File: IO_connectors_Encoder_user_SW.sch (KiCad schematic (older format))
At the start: 36 parts, among them IC1 TPD4E001DRLR, IC2 74AUP1G74DC.125, IC3 CD74HC4050PWR, SW1 TL1100CF160Q, SW2 PEC16-2215F-S0024, X1 DS1024-2*20R0, X2 DS1013-16SSIB1, X3 691322110005

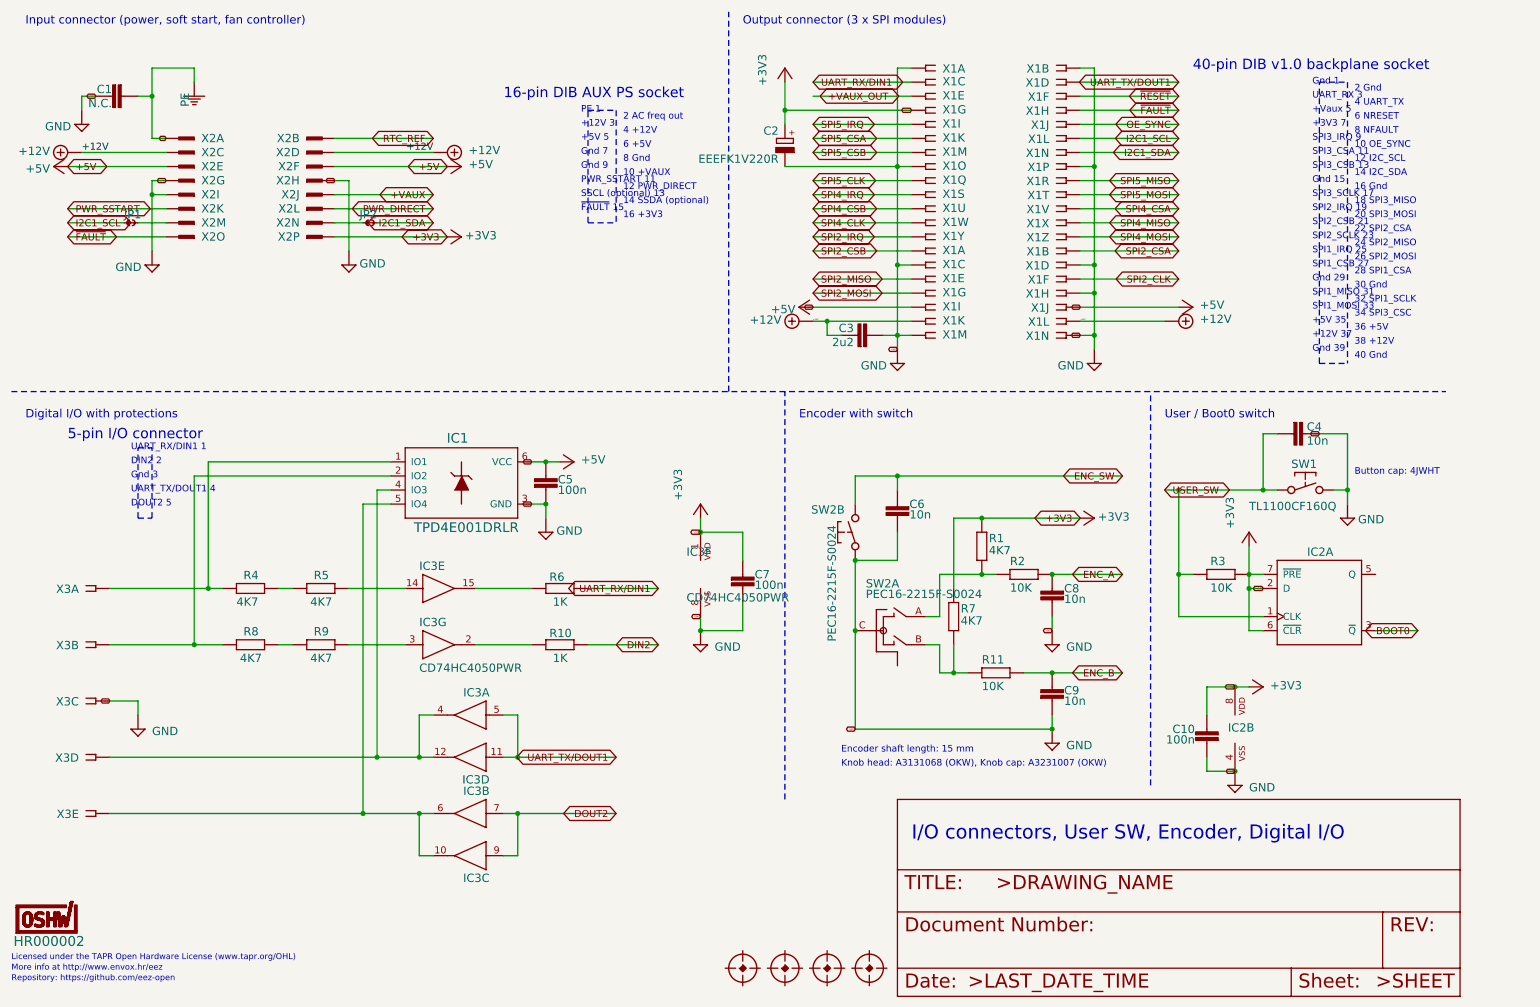
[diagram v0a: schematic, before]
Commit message: Assigning parts - netlitst to pcb
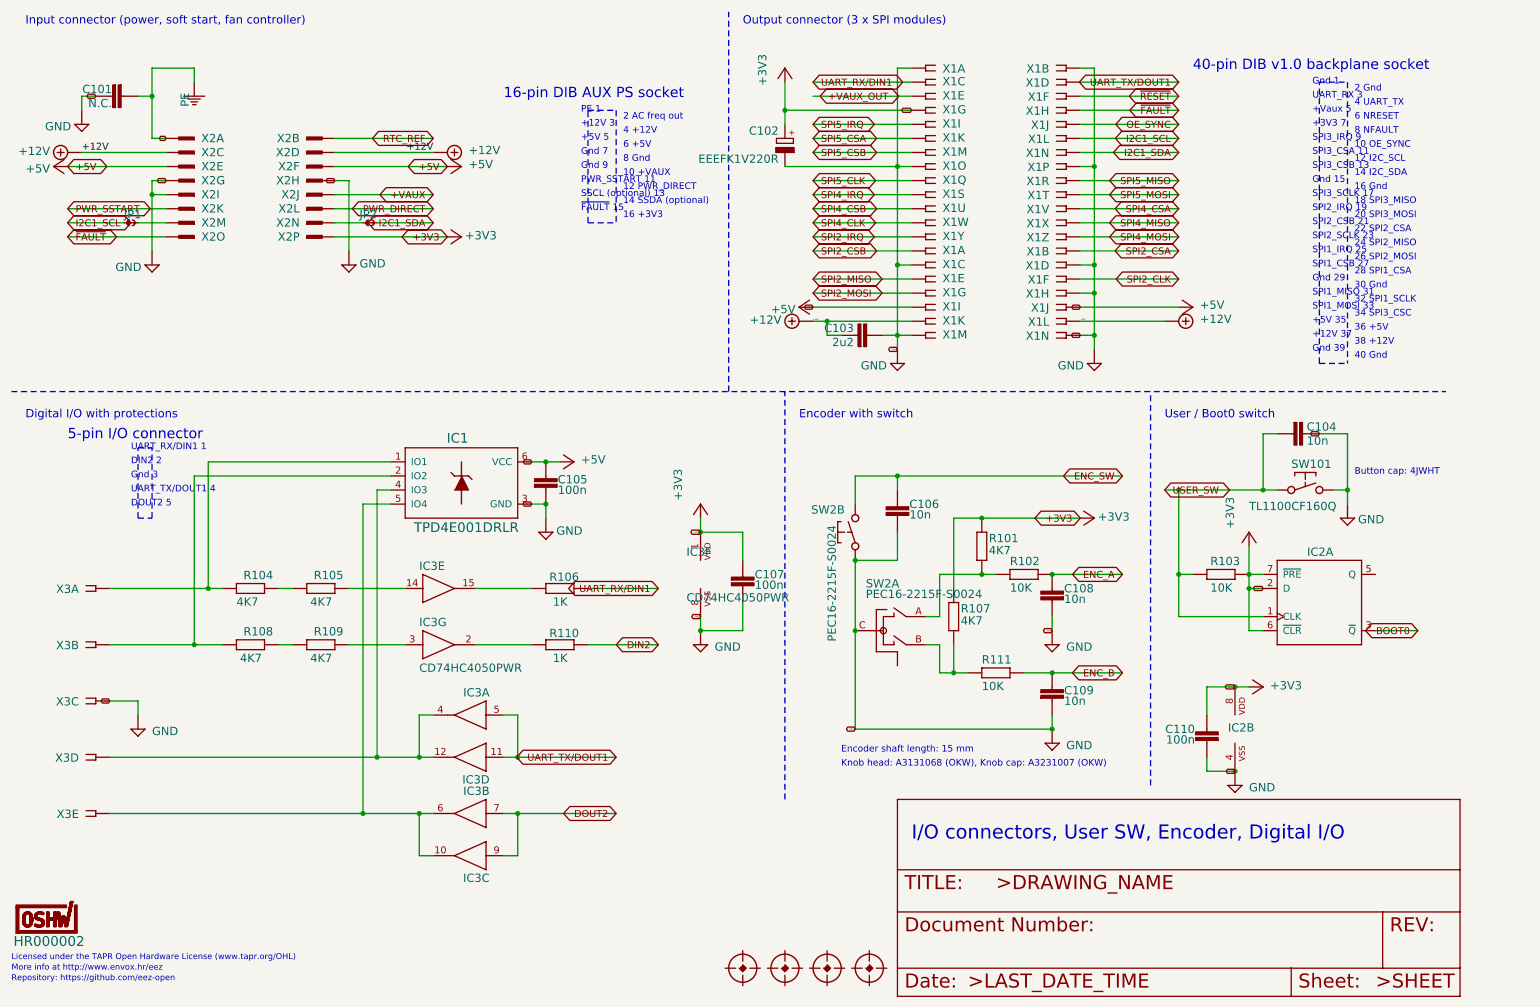
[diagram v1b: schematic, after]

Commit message: New annotation - All STM32 parts are +100
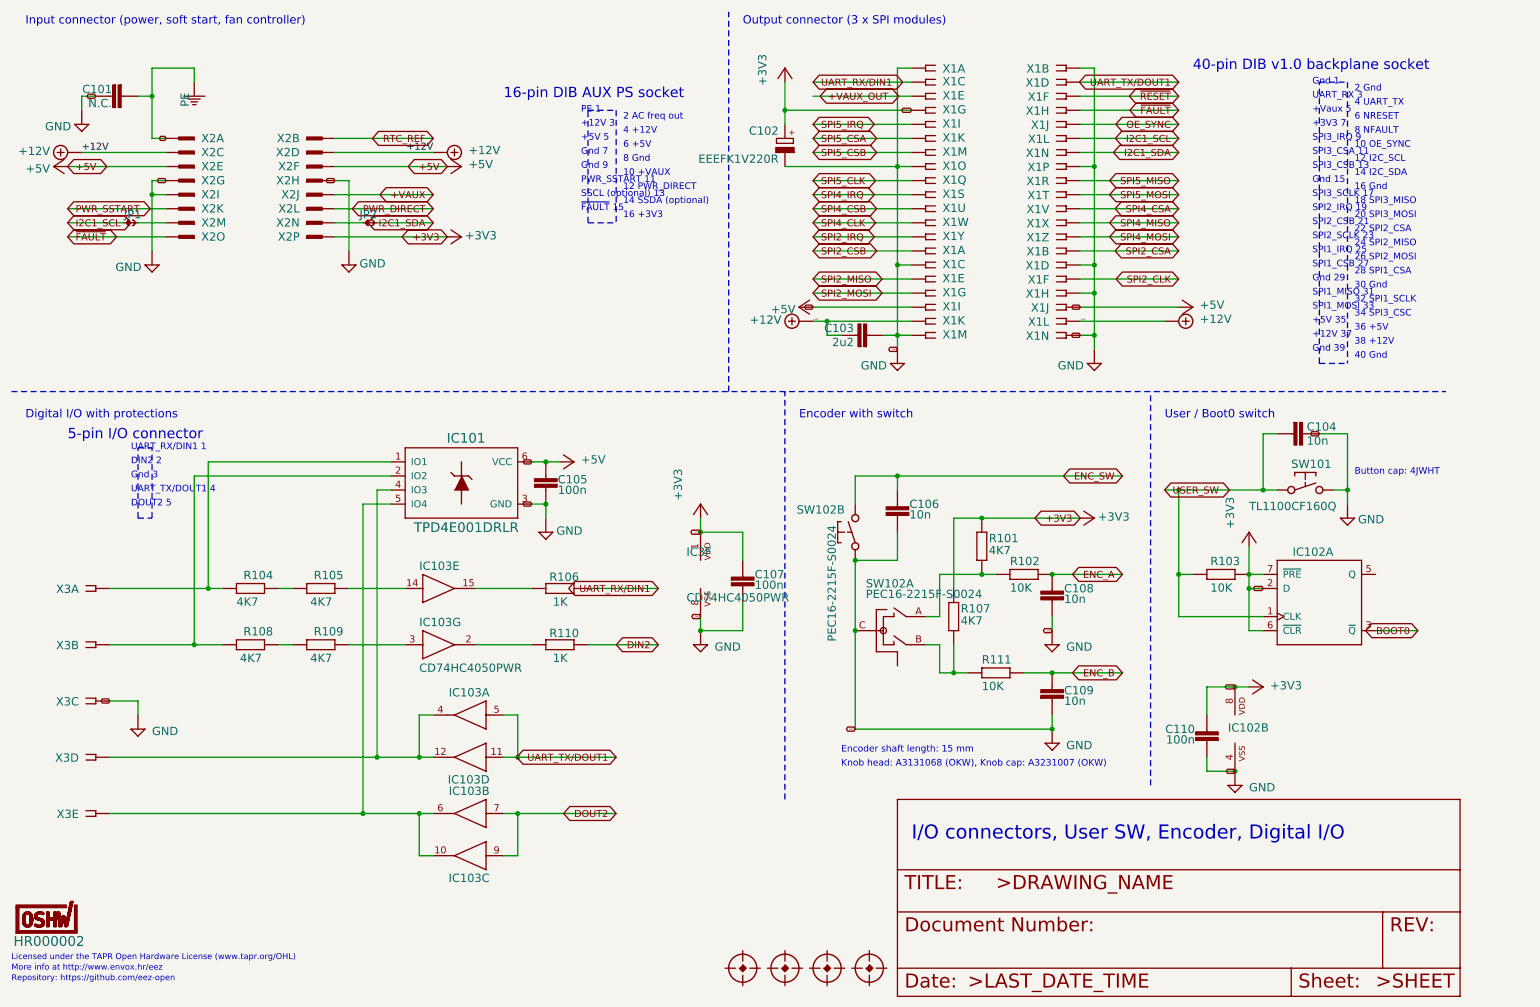
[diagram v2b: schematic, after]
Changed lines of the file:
@@
 EESchema Schematic File Version 4
-LIBS:ulx3s-cache
-EELAYER 29 0
+EELAYER 30 0
 EELAYER END
 $Descr User 12131 8568
@@
 AR Path="/C308D36B2E8B8105" Ref="SW2"  Part="1"
 AR Path="/5F88C8A0/C308D36B2E8B8105" Ref="SW2"  Part="1"
-AR Path="/5F8FDB74/2E8B8105" Ref="SW2"  Part="1"
-F 0 "SW2" H 7075 5400 59  0000 L BNN
+AR Path="/5F8FDB74/2E8B8105" Ref="SW102"  Part="1"
+F 0 "SW102" H 7075 5400 59  0000 L BNN
 F 1 "PEC16-2215F-S0024" H 7075 5325 59  0000 L BNN
 F 2 "EEZ DIB MCU r3B4:PEC16-2215F" H 7100 5100 50  0001 C CNN
@@
 AR Path="/C308D36B2E8B8109" Ref="SW2"  Part="2"
 AR Path="/5F88C8A0/C308D36B2E8B8109" Ref="SW2"  Part="2"
-AR Path="/5F8FDB74/2E8B8109" Ref="SW2"  Part="2"
-F 0 "SW2" V 7125 4475 59  0000 L TNN
+AR Path="/5F8FDB74/2E8B8109" Ref="SW102"  Part="2"
+F 0 "SW102" V 7125 4475 59  0000 L TNN
 F 1 "PEC16-2215F-S0024" H 7050 4600 59  0000 R TNN
 F 2 "EEZ DIB MCU r3B4:PEC16-2215F" H 7000 4400 50  0001 C CNN
@@
 AR Path="/B33006915ED25CA7" Ref="IC3"  Part="1"
 AR Path="/5F88C8A0/B33006915ED25CA7" Ref="IC3"  Part="1"
-AR Path="/5F8FDB74/5ED25CA7" Ref="IC3"  Part="1"
-F 0 "IC3" H 4200 5825 59  0000 L BNN
+AR Path="/5F8FDB74/5ED25CA7" Ref="IC103"  Part="1"
+F 0 "IC103" H 4200 5825 59  0000 L BNN
 F 1 "CD74HC4050PWR" H 4200 5500 59  0001 L BNN
 F 2 "EEZ DIB MCU r3B4:PW16" H 4300 5700 50  0001 C CNN
@@
 AR Path="/B33006915ED25CAB" Ref="IC3"  Part="2"
 AR Path="/5F88C8A0/B33006915ED25CAB" Ref="IC3"  Part="2"
-AR Path="/5F8FDB74/5ED25CAB" Ref="IC3"  Part="2"
-F 0 "IC3" H 4200 6525 59  0000 L BNN
+AR Path="/5F8FDB74/5ED25CAB" Ref="IC103"  Part="2"
+F 0 "IC103" H 4200 6525 59  0000 L BNN
 F 1 "CD74HC4050PWR" H 4200 6200 59  0001 L BNN
 F 2 "EEZ DIB MCU r3B4:PW16" H 4300 6400 50  0001 C CNN
@@
 AR Path="/B33006915ED25CAF" Ref="IC3"  Part="3"
 AR Path="/5F88C8A0/B33006915ED25CAF" Ref="IC3"  Part="3"
-AR Path="/5F8FDB74/5ED25CAF" Ref="IC3"  Part="3"
-F 0 "IC3" H 4200 6825 59  0000 L BNN
+AR Path="/5F8FDB74/5ED25CAF" Ref="IC103"  Part="3"
+F 0 "IC103" H 4200 6825 59  0000 L BNN
 F 1 "CD74HC4050PWR" H 4200 6500 59  0001 L BNN
 F 2 "EEZ DIB MCU r3B4:PW16" H 4300 6700 50  0001 C CNN
@@
 AR Path="/B33006915ED25CB3" Ref="IC3"  Part="4"
 AR Path="/5F88C8A0/B33006915ED25CB3" Ref="IC3"  Part="4"
-AR Path="/5F8FDB74/5ED25CB3" Ref="IC3"  Part="4"
-F 0 "IC3" H 4200 6125 59  0000 L BNN
+AR Path="/5F8FDB74/5ED25CB3" Ref="IC103"  Part="4"
+F 0 "IC103" H 4200 6125 59  0000 L BNN
 F 1 "CD74HC4050PWR" H 4200 5800 59  0001 L BNN
 F 2 "EEZ DIB MCU r3B4:PW16" H 4300 6000 50  0001 C CNN
@@
 AR Path="/B33006915ED25CBF" Ref="IC3"  Part="7"
 AR Path="/5F88C8A0/B33006915ED25CBF" Ref="IC3"  Part="7"
-AR Path="/5F8FDB74/5ED25CBF" Ref="IC3"  Part="7"
-F 0 "IC3" H 3900 5325 59  0000 L BNN
+AR Path="/5F8FDB74/5ED25CBF" Ref="IC103"  Part="7"
+F 0 "IC103" H 3900 5325 59  0000 L BNN
 F 1 "CD74HC4050PWR" H 3900 5000 59  0000 L BNN
 F 2 "EEZ DIB MCU r3B4:PW16" H 4000 5200 50  0001 C CNN
@@
 AR Path="/B33006915ED25CB7" Ref="IC3"  Part="5"
 AR Path="/5F88C8A0/B33006915ED25CB7" Ref="IC3"  Part="5"
-AR Path="/5F8FDB74/5ED25CB7" Ref="IC3"  Part="5"
-F 0 "IC3" H 3900 4925 59  0000 L BNN
+AR Path="/5F8FDB74/5ED25CB7" Ref="IC103"  Part="5"
+F 0 "IC103" H 3900 4925 59  0000 L BNN
 F 1 "CD74HC4050PWR" H 3900 4600 59  0001 L BNN
 F 2 "EEZ DIB MCU r3B4:PW16" H 4000 4800 50  0001 C CNN
@@
 AR Path="/A199DC2541D8E9F" Ref="IC1"  Part="1"
 AR Path="/5F88C8A0/A199DC2541D8E9F" Ref="IC1"  Part="1"
-AR Path="/5F8FDB74/541D8E9F" Ref="IC1"  Part="1"
-F 0 "IC1" H 4095 4228 69  0000 L BNN
+AR Path="/5F8FDB74/541D8E9F" Ref="IC101"  Part="1"
+F 0 "IC101" H 4095 4228 69  0000 L BNN
 F 1 "TPD4E001DRLR" H 3862 3593 69  0000 L BNN
 F 2 "EEZ DIB MCU r3B4:DRL6" H 4200 4000 50  0001 C CNN
@@
 AR Path="/279C899179298246" Ref="IC2"  Part="1"
 AR Path="/5F88C8A0/279C899179298246" Ref="IC2"  Part="1"
-AR Path="/5F8FDB74/79298246" Ref="IC2"  Part="1"
-F 0 "IC2" H 10400 5225 59  0000 R BNN
+AR Path="/5F8FDB74/79298246" Ref="IC102"  Part="1"
+F 0 "IC102" H 10400 5225 59  0000 R BNN
 F 1 "74AUP1G74DC.125" H 9900 4500 59  0001 L BNN
 F 2 "EEZ DIB MCU r3B4:DCU8" H 10300 4900 50  0001 C CNN
@@
 AR Path="/279C89917929824A" Ref="IC2"  Part="2"
 AR Path="/5F88C8A0/279C89917929824A" Ref="IC2"  Part="2"
-AR Path="/5F8FDB74/7929824A" Ref="IC2"  Part="2"
-F 0 "IC2" H 9650 5775 59  0000 L BNN
+AR Path="/5F8FDB74/7929824A" Ref="IC102"  Part="2"
+F 0 "IC102" H 9650 5775 59  0000 L BNN
 F 1 "74AUP1G74DC.125" H 9400 5400 59  0001 L BNN
 F 2 "EEZ DIB MCU r3B4:DCU8" H 9700 5800 50  0001 C CNN

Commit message: All STM32 parts are now +100, moving parts to original position
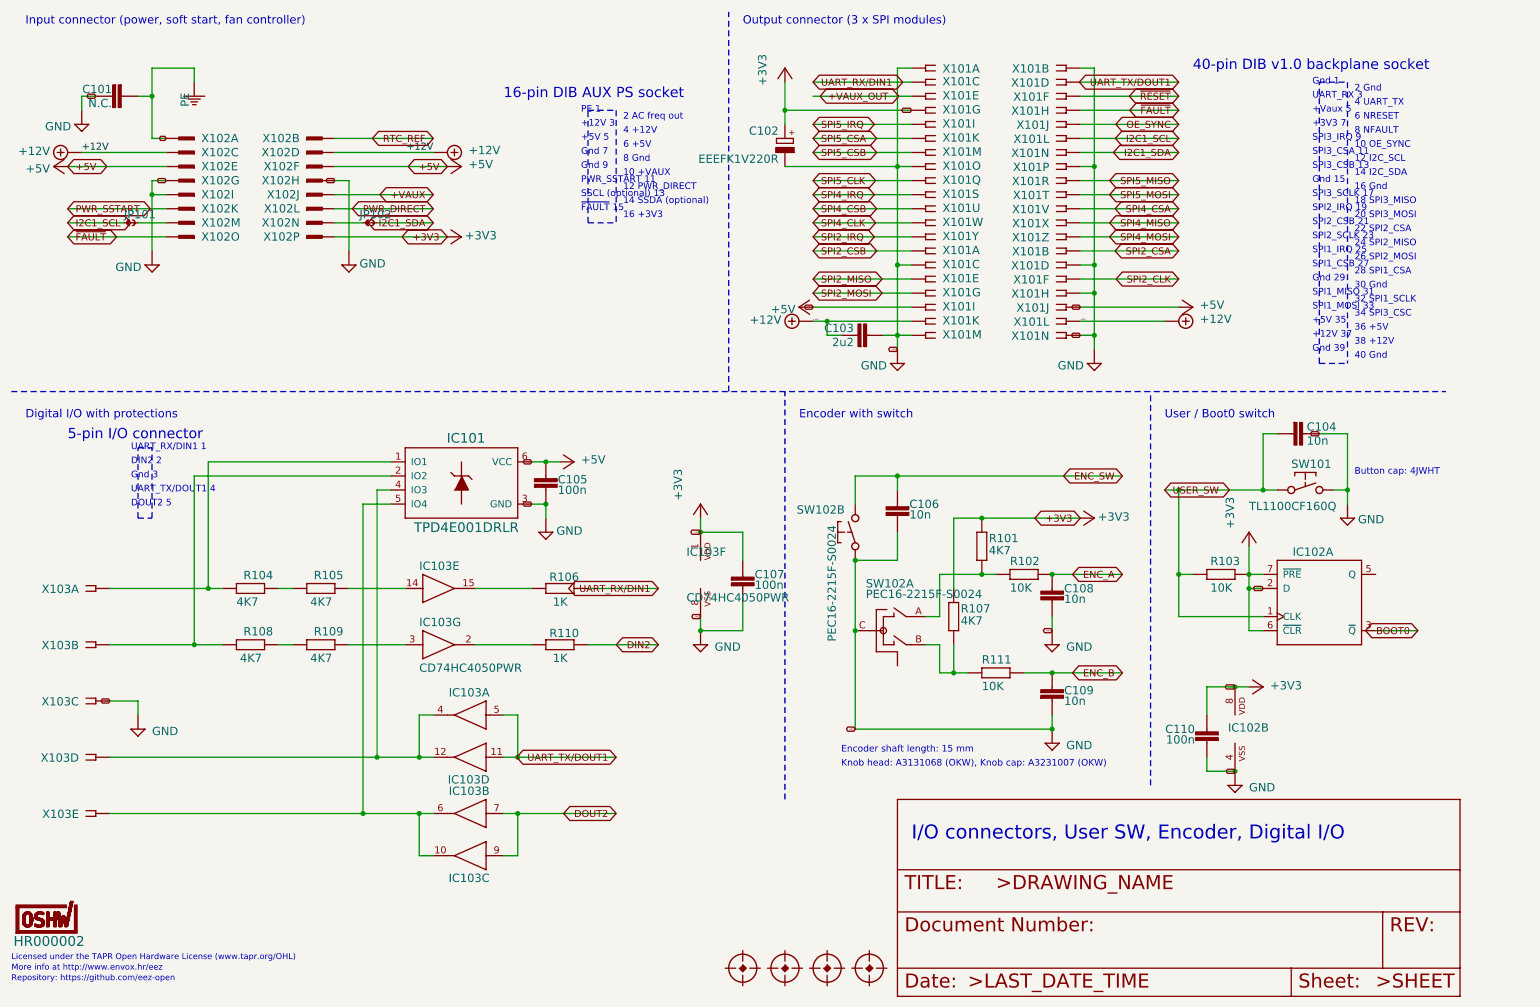
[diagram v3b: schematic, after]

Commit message: Adding default parts
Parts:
- C1, C3, C4, C6, C8, C9: footprint EEZ DIB MCU r3B4:C0805 -> Capacitor_SMD:C_0805_2012Metric
- C10, C5, C7: footprint EEZ DIB MCU r3B4:C0603 -> Capacitor_SMD:C_0603_1608Metric
- R1, R10, R11, R2, R3, R4, R5, R6, R7, R8, R9: footprint EEZ DIB MCU r3B4:R0805 -> Resistor_SMD:R_0805_2012Metric
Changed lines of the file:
@@
 F 0 "C108" H 8315 4835 59  0000 R TNN
 F 1 "10n" H 8315 4910 59  0000 R TNN
-F 2 "EEZ DIB MCU r3B4:C0805" H 8400 4900 50  0001 C CNN
+F 2 "Capacitor_SMD:C_0805_2012Metric" H 8400 4900 50  0001 C CNN
 F 3 "" H 8400 4900 50  0001 C CNN
 	1    8400 4900
@@
 F 0 "C109" H 8485 5440 59  0000 L BNN
 F 1 "10n" H 8485 5365 59  0000 L BNN
-F 2 "EEZ DIB MCU r3B4:C0805" H 8400 5500 50  0001 C CNN
+F 2 "Capacitor_SMD:C_0805_2012Metric" H 8400 5500 50  0001 C CNN
 F 3 "" H 8400 5500 50  0001 C CNN
 	1    8400 5500
@@
 F 0 "R102" H 8300 4759 59  0000 R BNN
 F 1 "10K" H 8300 4570 59  0000 R BNN
-F 2 "EEZ DIB MCU r3B4:R0805" H 8200 4700 50  0001 C CNN
+F 2 "Resistor_SMD:R_0805_2012Metric" H 8200 4700 50  0001 C CNN
 F 3 "" H 8200 4700 50  0001 C CNN
 	1    8200 4700
@@
 F 0 "R101" V 7809 4450 59  0000 R TNN
 F 1 "4K7" V 7895 4450 59  0000 R TNN
-F 2 "EEZ DIB MCU r3B4:R0805" H 7900 4500 50  0001 C CNN
+F 2 "Resistor_SMD:R_0805_2012Metric" H 7900 4500 50  0001 C CNN
 F 3 "" H 7900 4500 50  0001 C CNN
 	1    7900 4500
@@
 F 0 "R107" V 7609 4950 59  0000 R TNN
 F 1 "4K7" V 7695 4950 59  0000 R TNN
-F 2 "EEZ DIB MCU r3B4:R0805" H 7700 5000 50  0001 C CNN
+F 2 "Resistor_SMD:R_0805_2012Metric" H 7700 5000 50  0001 C CNN
 F 3 "" H 7700 5000 50  0001 C CNN
 	1    7700 5000
@@
 F 0 "R111" H 8100 5459 59  0000 R BNN
 F 1 "10K" H 8100 5270 59  0000 R BNN
-F 2 "EEZ DIB MCU r3B4:R0805" H 8000 5400 50  0001 C CNN
+F 2 "Resistor_SMD:R_0805_2012Metric" H 8000 5400 50  0001 C CNN
 F 3 "" H 8000 5400 50  0001 C CNN
 	1    8000 5400
@@
 F 0 "C106" H 7215 4235 59  0000 R TNN
 F 1 "10n" H 7215 4310 59  0000 R TNN
-F 2 "EEZ DIB MCU r3B4:C0805" H 7300 4300 50  0001 C CNN
+F 2 "Capacitor_SMD:C_0805_2012Metric" H 7300 4300 50  0001 C CNN
 F 3 "" H 7300 4300 50  0001 C CNN
 	1    7300 4300
@@
 F 0 "C104" V 10185 3710 59  0000 L BNN
 F 1 "10n" V 10285 3710 59  0000 L BNN
-F 2 "EEZ DIB MCU r3B4:C0805" H 10200 3700 50  0001 C CNN
+F 2 "Capacitor_SMD:C_0805_2012Metric" H 10200 3700 50  0001 C CNN
 F 3 "" H 10200 3700 50  0001 C CNN
 	1    10200 3700
@@
 F 0 "R105" H 3150 4741 59  0000 L TNN
 F 1 "4K7" H 3125 4930 59  0000 L TNN
-F 2 "EEZ DIB MCU r3B4:R0805" H 3200 4800 50  0001 C CNN
+F 2 "Resistor_SMD:R_0805_2012Metric" H 3200 4800 50  0001 C CNN
 F 3 "" H 3200 4800 50  0001 C CNN
 	1    3200 4800
@@
 F 0 "R104" H 2650 4741 59  0000 L TNN
 F 1 "4K7" H 2600 4930 59  0000 L TNN
-F 2 "EEZ DIB MCU r3B4:R0805" H 2700 4800 50  0001 C CNN
+F 2 "Resistor_SMD:R_0805_2012Metric" H 2700 4800 50  0001 C CNN
 F 3 "" H 2700 4800 50  0001 C CNN
 	1    2700 4800
@@
 F 0 "R109" H 3150 5141 59  0000 L TNN
 F 1 "4K7" H 3125 5330 59  0000 L TNN
-F 2 "EEZ DIB MCU r3B4:R0805" H 3200 5200 50  0001 C CNN
+F 2 "Resistor_SMD:R_0805_2012Metric" H 3200 5200 50  0001 C CNN
 F 3 "" H 3200 5200 50  0001 C CNN
 	1    3200 5200
@@
 F 0 "R108" H 2650 5141 59  0000 L TNN
 F 1 "4K7" H 2625 5330 59  0000 L TNN
-F 2 "EEZ DIB MCU r3B4:R0805" H 2700 5200 50  0001 C CNN
+F 2 "Resistor_SMD:R_0805_2012Metric" H 2700 5200 50  0001 C CNN
 F 3 "" H 2700 5200 50  0001 C CNN
 	1    2700 5200
@@
 F 0 "C107" H 6285 4665 59  0000 L BNN
 F 1 "100n" H 6285 4590 59  0000 L BNN
-F 2 "EEZ DIB MCU r3B4:C0603" H 6200 4700 50  0001 C CNN
+F 2 "Capacitor_SMD:C_0603_1608Metric" H 6200 4700 50  0001 C CNN
 F 3 "" H 6200 4700 50  0001 C CNN
 	1    6200 4700
@@
 F 0 "R106" H 4825 4684 59  0000 L BNN
 F 1 "1K" H 4850 4930 59  0000 L TNN
-F 2 "EEZ DIB MCU r3B4:R0805" H 4900 4800 50  0001 C CNN
+F 2 "Resistor_SMD:R_0805_2012Metric" H 4900 4800 50  0001 C CNN
 F 3 "" H 4900 4800 50  0001 C CNN
 	1    4900 4800
@@
 F 0 "R110" H 4825 5084 59  0000 L BNN
 F 1 "1K" H 4850 5330 59  0000 L TNN
-F 2 "EEZ DIB MCU r3B4:R0805" H 4900 5200 50  0001 C CNN
+F 2 "Resistor_SMD:R_0805_2012Metric" H 4900 5200 50  0001 C CNN
 F 3 "" H 4900 5200 50  0001 C CNN
 	1    4900 5200
@@
 F 0 "C105" H 4885 3940 59  0000 L BNN
 F 1 "100n" H 4885 3865 59  0000 L BNN
-F 2 "EEZ DIB MCU r3B4:C0603" H 4800 4000 50  0001 C CNN
+F 2 "Capacitor_SMD:C_0603_1608Metric" H 4800 4000 50  0001 C CNN
 F 3 "" H 4800 4000 50  0001 C CNN
 	1    4800 4000
@@
 F 0 "R103" H 9675 4641 59  0000 R TNN
 F 1 "10K" H 9675 4830 59  0000 R TNN
-F 2 "EEZ DIB MCU r3B4:R0805" H 9600 4700 50  0001 C CNN
+F 2 "Resistor_SMD:R_0805_2012Metric" H 9600 4700 50  0001 C CNN
 F 3 "" H 9600 4700 50  0001 C CNN
 	1    9600 4700
@@
 F 0 "C110" H 9585 5765 59  0000 L BNN
 F 1 "100n" H 9585 5690 59  0000 L BNN
-F 2 "EEZ DIB MCU r3B4:C0603" H 9500 5800 50  0001 C CNN
+F 2 "Capacitor_SMD:C_0603_1608Metric" H 9500 5800 50  0001 C CNN
 F 3 "" H 9500 5800 50  0001 C CNN
 	1    9500 5800
@@
 F 0 "C101" V 1685 1285 59  0000 L BNN
 F 1 "N.C." V 1785 1285 59  0000 L BNN
-F 2 "EEZ DIB MCU r3B4:C0805" H 1700 1300 50  0001 C CNN
+F 2 "Capacitor_SMD:C_0805_2012Metric" H 1700 1300 50  0001 C CNN
 F 3 "" H 1700 1300 50  0001 C CNN
 	1    1700 1300
@@
 F 0 "C103" V 7085 3010 59  0000 L BNN
 F 1 "2u2" V 6985 3010 59  0000 L BNN
-F 2 "EEZ DIB MCU r3B4:C0805" H 7000 3000 50  0001 C CNN
+F 2 "Capacitor_SMD:C_0805_2012Metric" H 7000 3000 50  0001 C CNN
 F 3 "" H 7000 3000 50  0001 C CNN
 	1    7000 3000
